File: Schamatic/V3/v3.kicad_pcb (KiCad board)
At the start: 2 copper layers, 51.6 x 27.9 mm, 29 parts, among them J1 SWD, J2 SENSOR, J3 CAN, Q1 PSMN014-40YS, Q2 PSMN014-40YS, Q3 PSMN014-40YS, Q4 PSMN014-40YS, Q5 PSMN014-40YS, Q6 PSMN014-40YS, U1 STSPIN32F0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

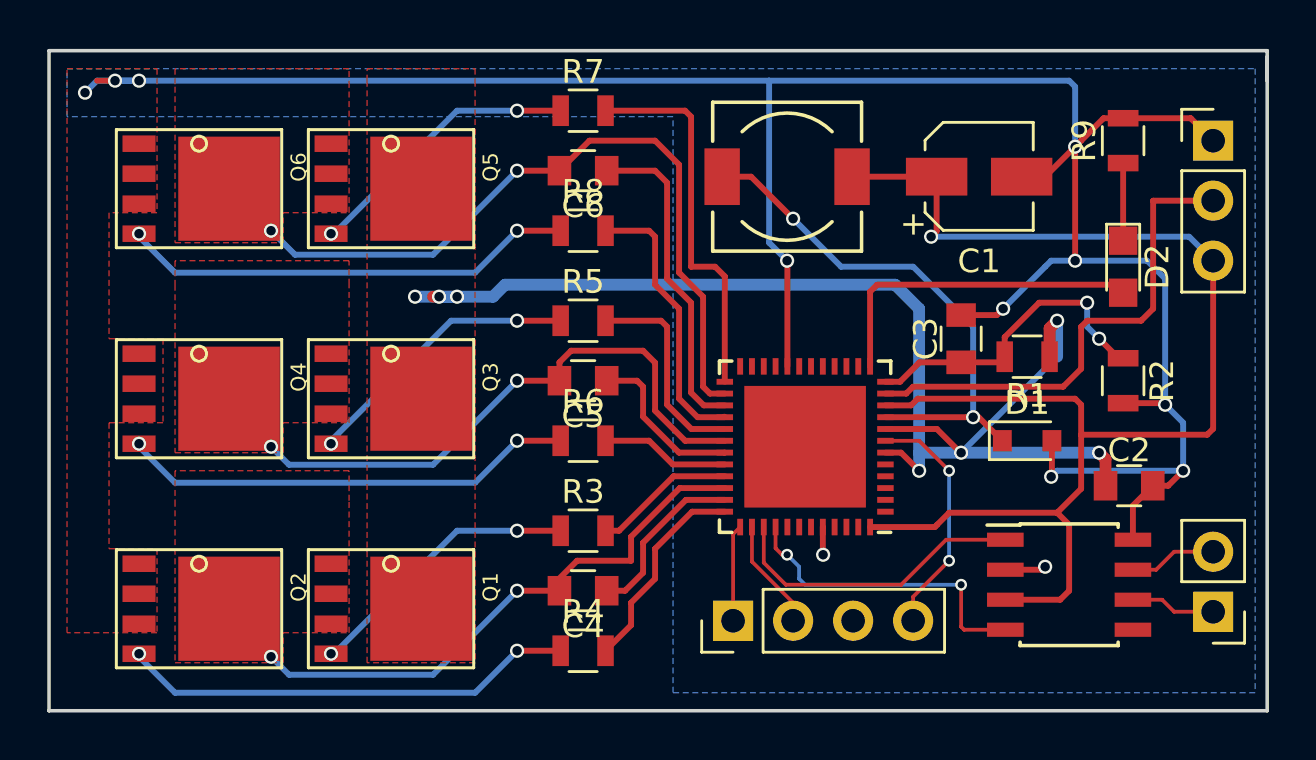
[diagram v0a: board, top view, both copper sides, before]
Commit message: board ordered
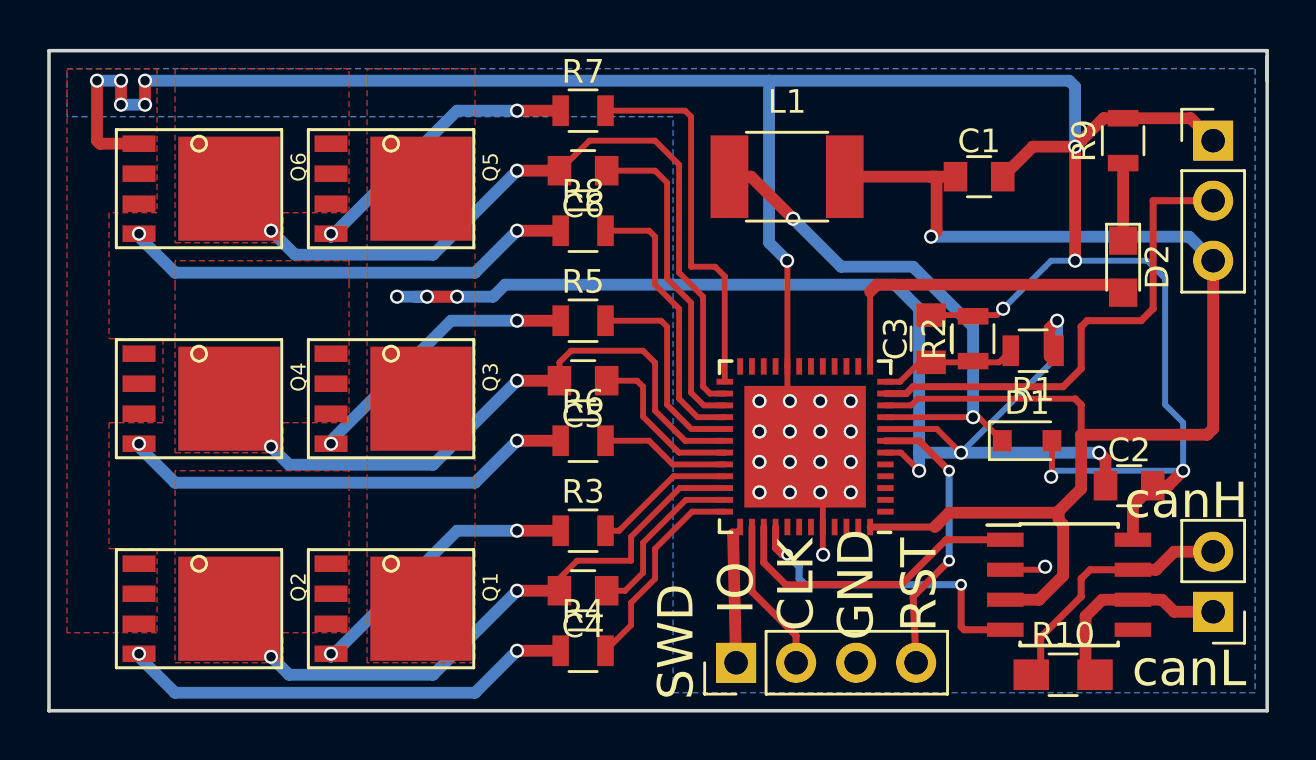
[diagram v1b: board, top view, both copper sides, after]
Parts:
- added R10: 120, Resistors_SMD:R_0805_HandSoldering, F.Cu at (162.6, 114.0)
- C1: footprint Capacitors_SMD:CP_Elec_4x4.5 -> Capacitors_SMD:C_0805
- C2, C3, C4, C5, C6: value C_Small -> 1uF
- L1: footprint Choke_SMD:Choke_SMD_6.3x6.3_H3 -> Inductors_SMD:L_1812
- Q1, Q2, Q3, Q4, Q5, Q6: value PSMN014-40YS -> PSMN3R3-40YS
- R1: value R -> 47K
- R2: value R -> 10K
- R3, R4, R5, R6, R7, R8: value R -> 10
- R9: value R -> 120
- moved R2 6.59 mm to (158.8, 99.8), turned to 90 degrees
- moved J1 1.78 mm to (148.7, 113.5)
- moved C3 1.27 mm to (157.0, 99.8)
- moved R1 0.36 mm to (161.3, 100.3)
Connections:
- U1 pad 49: (no net) -> Earth
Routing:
- net Earth: track 108.5 -> 137.1 mm, vias 12 -> 29
- net Net-(C3-Pad1): track 13.5 -> 5.49 mm, vias 2 -> 0
- net CANH: track 3.71 -> 10.8 mm
- net CANL: track 3.61 -> 8.37 mm
- net SWDCLK: track 4.69 -> 7.28 mm
- net NRST: track 10.2 -> 12.0 mm
- net SWDIO: track 4.09 -> 5.87 mm
- net +12V: track 53.3 -> 54.8 mm
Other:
- board text added: "CLK"
- board text added: "GND"
- board text added: "IO"
- board text added: "RST"
- board text added: "SWD"
- board text added: "canH"
- board text added: "canL"
